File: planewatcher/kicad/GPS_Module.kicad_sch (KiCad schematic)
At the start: 9 parts, among them U1 LEA-M8T

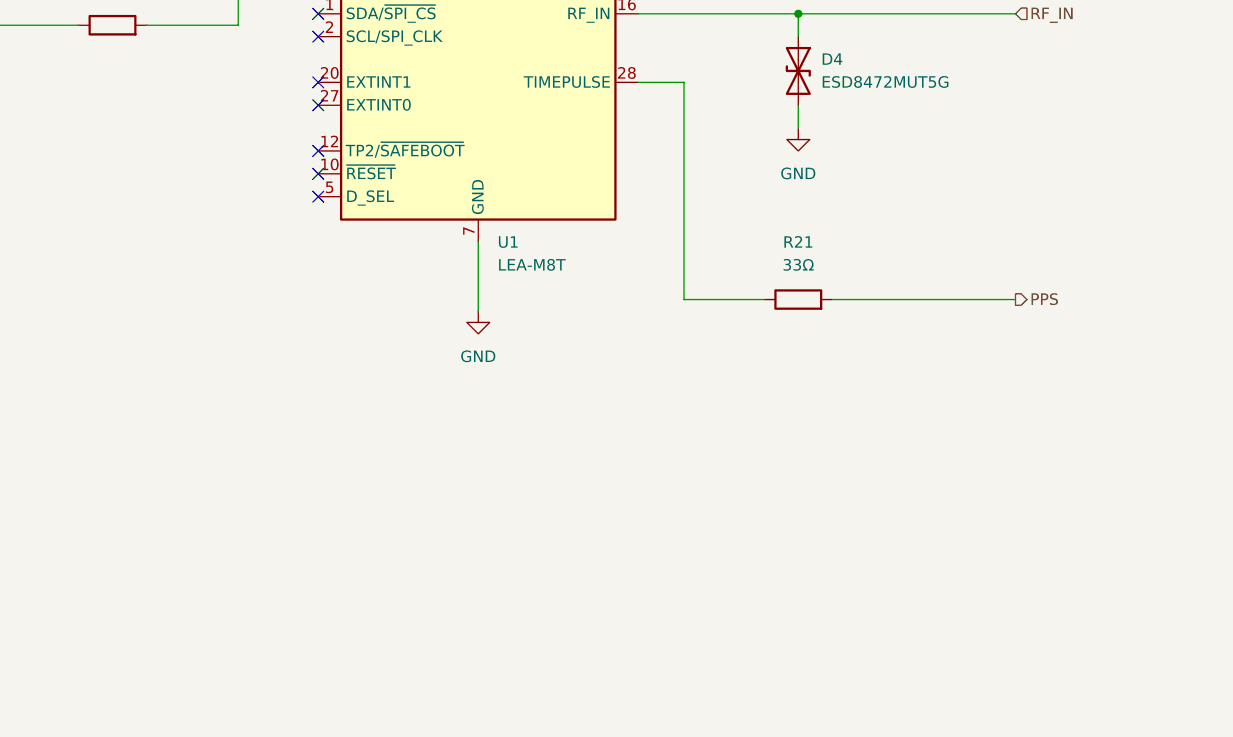
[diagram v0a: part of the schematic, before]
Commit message: add pink led for gps pps + attach gps reset to fpga
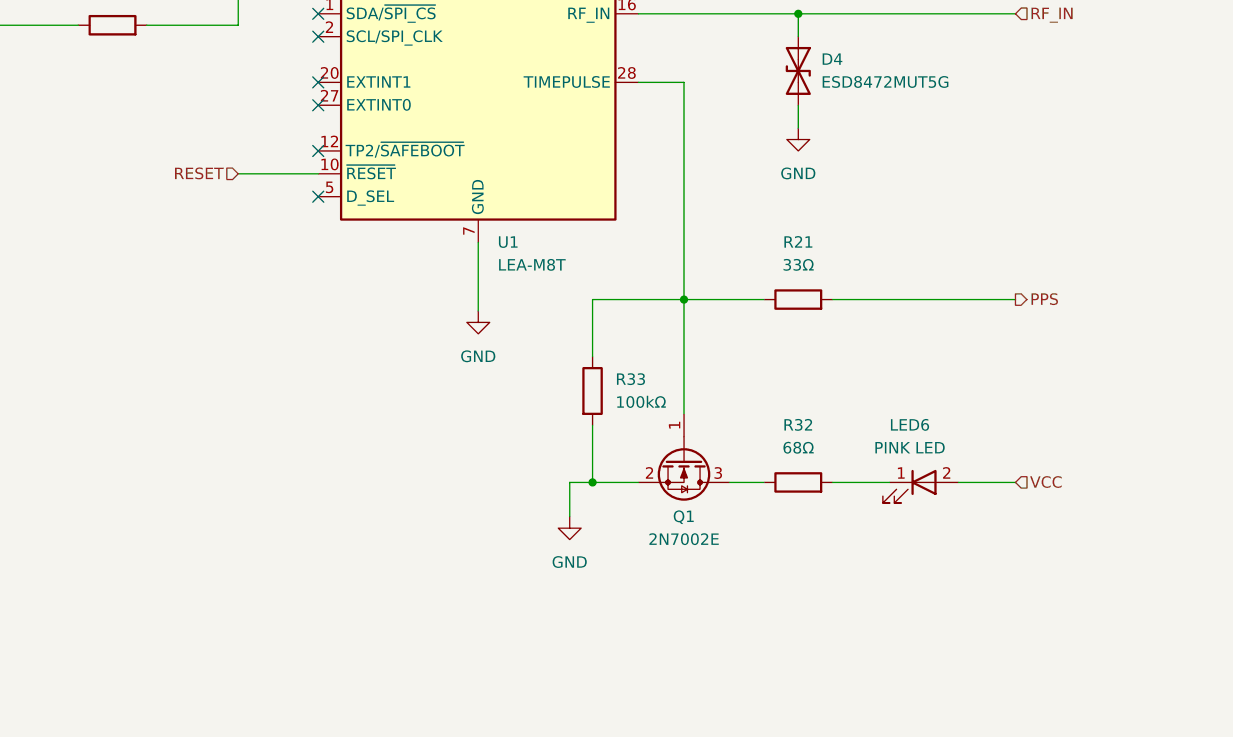
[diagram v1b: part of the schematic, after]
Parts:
- added LED6: PINK LED, LED_SMD:LED_0603_1608Metric, symbol Device:LED
- added Q1: 2N7002E, Package_TO_SOT_SMD:SOT-23, symbol Transistor_FET:2N7002E
- added R32: 68Ω, Resistor_SMD:R_0402_1005Metric, symbol Device:R
- added R33: 100kΩ, Resistor_SMD:R_0402_1005Metric, symbol Device:R
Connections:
- net GND: now also Q1.2 (S), R33.2
- net VCC: now also LED6.2 (A)
- net at R21.1, U1.28 (TIMEPULSE): now also Q1.1 (G), R33.1
- net RESET: now reaches U1.10 (~{RESET})
- new net: Q1.3 (D), R32.1
- new net: LED6.1 (K), R32.2
- no-connect marks 10 -> 9

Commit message: Add bias-tee power switch & connect GPS TP2
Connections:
- net TP2: now reaches U1.12 (TP2/~{SAFEBOOT})
- no-connect marks 9 -> 8
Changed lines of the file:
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@@
-	)
-	(no_connect
-		(at 130.81 110.49)
 	)
 	(no_connect
@@
 		(pts
 			(xy 111.76 81.28) (xy 121.92 81.28)
+		)
+		(stroke
+			(width 0)
+			(type default)
+		)
+	)
+	(wire
+		(pts
+			(xy 121.92 110.49) (xy 130.81 110.49)
 		)
 		(stroke
@@
 		)
 	)
+	(hierarchical_label "TP2"
+		(shape tri_state)
+		(at 121.92 110.49 180)
+		(effects
+			(font
+				(size 1.27 1.27)
+			)
+			(justify right)
+		)
+	)

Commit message: Decrease brightness of PPS LED
Bump up series resistor to 1kΩ from 58Ω (lol)
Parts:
- R32: value 68Ω -> 1kΩ; MPN ERJPA2F68R0X -> (none); Manufacturer PANASONIC -> (none); lcsc_id C542959 -> (none)
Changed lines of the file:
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@@
 			)
 		)
-		(property "Value" "68Ω"
+		(property "Value" "1kΩ"
 			(at 184.15 143.51 90)
 			(show_name no)
@@
 			)
 		)
-		(property "Description" "68Ω 200mW Thick Film Resistor ±100ppm/℃ ±1% 0402 Chip Resistor - Surface Mount RoHS"
+		(property "Description" ""
 			(at 184.15 147.32 0)
 			(hide yes)
@@
 			)
 		)
-		(property "MPN" "ERJPA2F68R0X"
+		(property "MPN" ""
 			(at 184.15 147.32 90)
 			(hide yes)
@@
 			)
 		)
-		(property "Manufacturer" "PANASONIC"
+		(property "Manufacturer" ""
 			(at 184.15 147.32 90)
 			(hide yes)
@@
 			)
 		)
-		(property "lcsc_id" "C542959"
+		(property "lcsc_id" ""
 			(at 184.15 147.32 90)
 			(hide yes)

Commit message: Add optional PPS output
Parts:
- removed Q1: 2N7002E, Package_TO_SOT_SMD:SOT-23, symbol Transistor_FET:2N7002E
- added C62: 100nF, Capacitor_SMD:C_0402_1005Metric, symbol Device:C
- added C63: 4.7µF, Capacitor_SMD:C_0603_1608Metric, symbol Device:C
- added D5: ESD8472MUT5G, Diode_SMD:D_0201_0603Metric, symbol Device:D_TVS
- added J1: 1PPS_OUT, Connector_Coaxial:U.FL_Hirose_U.FL-R-SMT-1_Vertical, symbol Connector:Conn_Coaxial
- added R47: 100kΩ, Resistor_SMD:R_0402_1005Metric, symbol Device:R
- added U4: TC4427xOA, Package_SO:SOIC-8_3.9x4.9mm_P1.27mm, symbol Driver_FET:TC4427xOA
- LED6: Purpose Flashes 1PPS from GPS module -> Visual 1PPS activity indicator. Blinks when GPS TIMEPULSE i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
- R21: Purpose Series damping/termination for GPS module digital I/O lines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 -> Small series resistor feeding FPGA PPS input. Provides edge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
- R32: value 1kΩ -> 2.2kΩ; MPN (none) -> CRCW04022K20JNED; Manufacturer (none) -> VISHAY; Purpose Series resistor for GPS timepulse pink LED. -> LED current-limiting resistor. Sets the 1PPS indicator brig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; lcsc_id (none) -> C4202009
- R33: value 100kΩ -> 49.9Ω 0.5W; footprint Resistor_SMD:R_0402_1005Metric -> Resistor_SMD:R_0805_2012Metric; MPN RC0402FR-07100KL -> ERJP06F49R9V; Manufacturer YAGEO -> PANASONIC; Package 0402 (1005 Metric) -> 0805 (2012 Metric); Purpose Gate pull-down for FET. -> Source-termination / current-limiting resistor for the 1PPS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; lcsc_id C60491 -> C77379
- U1: MPN (none) -> LEA-M8T; Manufacturer (none) -> U-BLOX; lcsc_id (none) -> C2763452
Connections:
- net GND: now also R32.1, C62.2, C63.2, D5.2 (A2), J1.2 (Ext), R47.2, U4.3 (GND); no longer R33.2
- net at R21.1, U1.28 (TIMEPULSE): now also R47.1, U4.2 (IN_A), U4.4 (IN_B); no longer R33.1
- net VCC renamed 3V3
- net 3V3: no longer LED6.2 (A)
- new net: D5.1 (A1), J1.1 (In), R33.2
- new net: LED6.2 (A), U4.5 (OUT_B)
- new net: R33.1, U4.7 (OUT_A)
- new net 5V: C62.1, C63.1, U4.6 (V_{DD})
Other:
- moved on the sheet: C59, C60, C74, D4, LED6, R20, R21, R23, R24, R32, U1

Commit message: Update PCB to include PPS output
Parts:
- U4: footprint Package_SO:SOIC-8_3.9x4.9mm_P1.27mm -> Package_SO:MSOP-8_3x3mm_P0.65mm; MPN TC4427AEOA713 -> TC4427EUA713; Package SOIC-8 -> MSOP-8; lcsc_id C20551 -> C628550
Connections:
- net 5V renamed 4V5
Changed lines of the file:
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@@
+	)
+	(junction
+		(at 85.09 53.34)
+		(diameter 0)
+		(color 0 0 0 0)
 	)
 	(junction
@@
 	(wire
 		(pts
-			(xy 83.82 53.34) (xy 90.17 53.34)
+			(xy 83.82 53.34) (xy 85.09 53.34)
 		)
 		(stroke
@@
 	(wire
 		(pts
+			(xy 85.09 53.34) (xy 90.17 53.34)
+		)
+		(stroke
+			(width 0)
+			(type default)
+		)
+	)
+	(wire
+		(pts
 			(xy 83.82 29.21) (xy 83.82 31.75)
 		)
@@
 		(pts
 			(xy 86.36 58.42) (xy 86.36 63.5)
+		)
+		(stroke
+			(width 0)
+			(type default)
+		)
+	)
+	(wire
+		(pts
+			(xy 85.09 52.07) (xy 85.09 53.34)
 		)
 		(stroke
@@
 		)
 	)
-	(hierarchical_label "5V"
+	(hierarchical_label "4V5"
 		(shape input)
 		(at 148.59 83.82 180)
@@
 				(path "/7a4a4324-e8b8-4d06-b75a-28095d4e9f10/84812100-48e5-47cc-a358-d48bbae76aaf"
 					(reference "C59")
+					(unit 1)
+				)
+			)
+		)
+	)
+	(symbol
+		(lib_id "power:PWR_FLAG")
+		(at 85.09 52.07 0)
+		(unit 1)
+		(body_style 1)
+		(exclude_from_sim no)
+		(in_bom yes)
+		(on_board yes)
+		(in_pos_files yes)
+		(dnp no)
+		(fields_autoplaced yes)
+		(property "Reference" "#FLG03"
+			(at 85.09 50.165 0)
+			(hide yes)
+			(show_name no)
+			(do_not_autoplace no)
+			(effects
+				(font
+					(size 1.27 1.27)
+				)
+			)
+		)
+		(property "Value" "PWR_FLAG"
+			(at 85.09 46.99 0)
+			(show_name no)
+			(do_not_autoplace no)
+			(effects
+				(font
+					(size 1.27 1.27)
+				)
+			)
+		)
+		(property "Footprint" ""
+			(at 85.09 52.07 0)
+			(hide yes)
+			(show_name no)
+			(do_not_autoplace no)
+			(effects
+				(font
+					(size 1.27 1.27)
+				)
+			)
+		)
+		(property "Datasheet" ""
+			(at 85.09 52.07 0)
+			(hide yes)
+			(show_name no)
+			(do_not_autoplace no)
+			(effects
+				(font
+					(size 1.27 1.27)
+				)
+			)
+		)
+		(property "Description" "Special symbol for telling ERC where power comes from"
+			(at 85.09 52.07 0)
+			(hide yes)
+			(show_name no)
+			(do_not_autoplace no)
+			(effects
+				(font
+					(size 1.27 1.27)
+				)
+			)
+		)
+		(pin "1"
+		)
+		(instances
+			(project "planewatcher"
+				(path "/7a4a4324-e8b8-4d06-b75a-28095d4e9f10/84812100-48e5-47cc-a358-d48bbae76aaf"
+					(reference "#FLG03")
 					(unit 1)
 				)
@@
 			)
 		)
-		(property "Footprint" "Package_SO:SOIC-8_3.9x4.9mm_P1.27mm"
+		(property "Footprint" "Package_SO:MSOP-8_3x3mm_P0.65mm"
 			(at 155.448 128.27 0)
 			(hide yes)
@@
 			)
 		)
-		(property "MPN" "TC4427AEOA713"
+		(property "MPN" "TC4427EUA713"
 			(at 154.94 113.03 0)
 			(hide yes)
@@
 			)
 		)
-		(property "Package" "SOIC-8"
+		(property "Package" "MSOP-8"
 			(at 154.94 113.03 0)
 			(hide yes)
@@
 			)
 		)
-		(property "lcsc_id" "C20551"
+		(property "lcsc_id" "C628550"
 			(at 154.94 113.03 0)
 			(hide yes)
